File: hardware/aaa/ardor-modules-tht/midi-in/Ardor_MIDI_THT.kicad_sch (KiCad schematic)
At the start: 18 parts, among them J101 POWER INPUT + UART OUTPUT TO 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, J202 MIDI INPUT FROM DIN SOCKET, J203 METAL CASE BOND + GROUND, U201 onsemi H11L1M

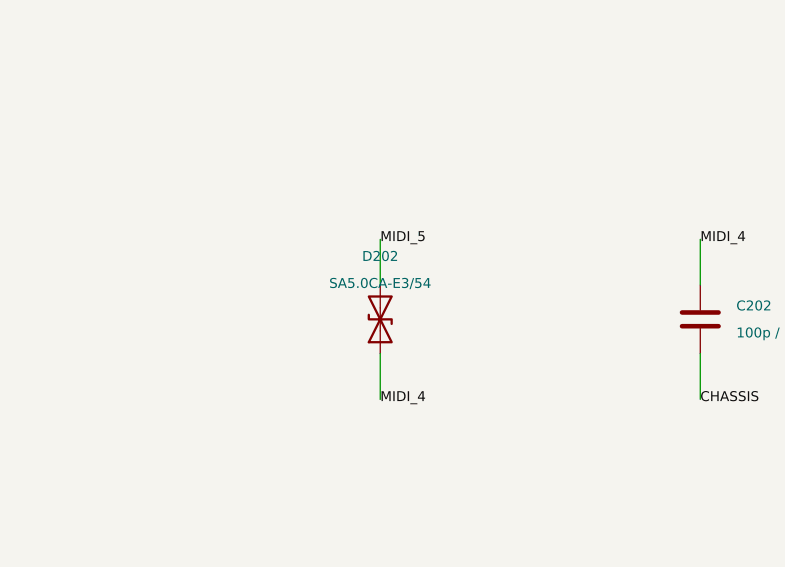
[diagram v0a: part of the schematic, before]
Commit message: fix(hardware): use Hestore TVS diodes in hand-assembly modules
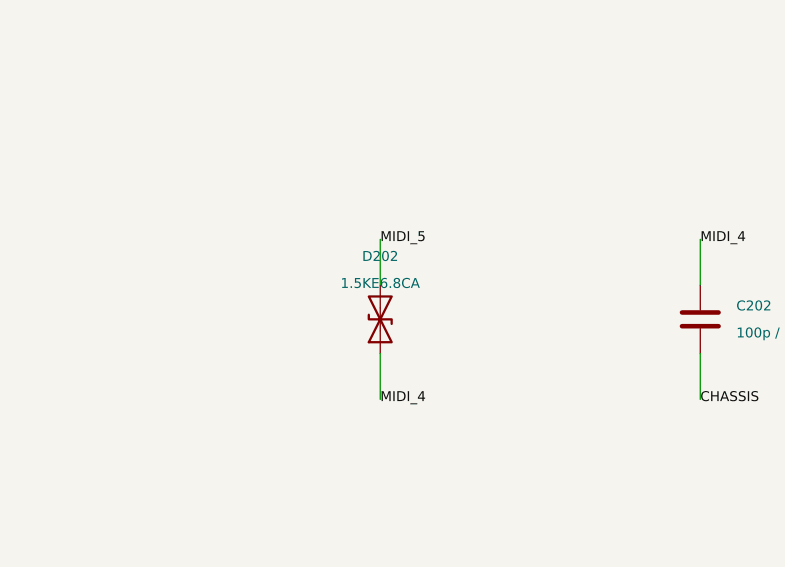
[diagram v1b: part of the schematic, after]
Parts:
- D202: value SA5.0CA-E3/54 -> 1.5KE6.8CA; footprint Diode_THT:D_DO-15_P10.16mm_Horizontal -> Ardor_THT:D_TVS_DC_1.5KE_P15.24mm; MPN Vishay SA5.0CA-E3/54 -> DC Components 1.5KE6.8CA (HESTORE 100.430.71)

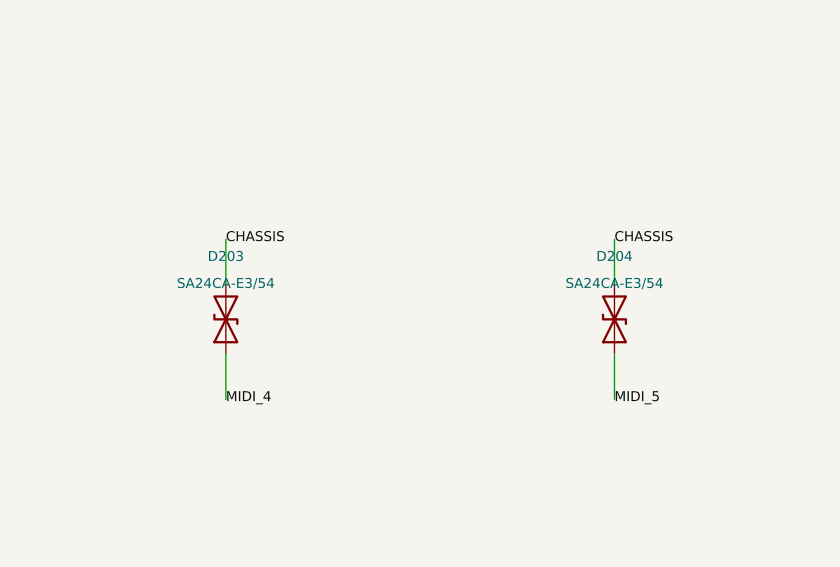
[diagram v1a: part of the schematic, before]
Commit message: feat(hardware): compact layouts and adopt Hestore module packages
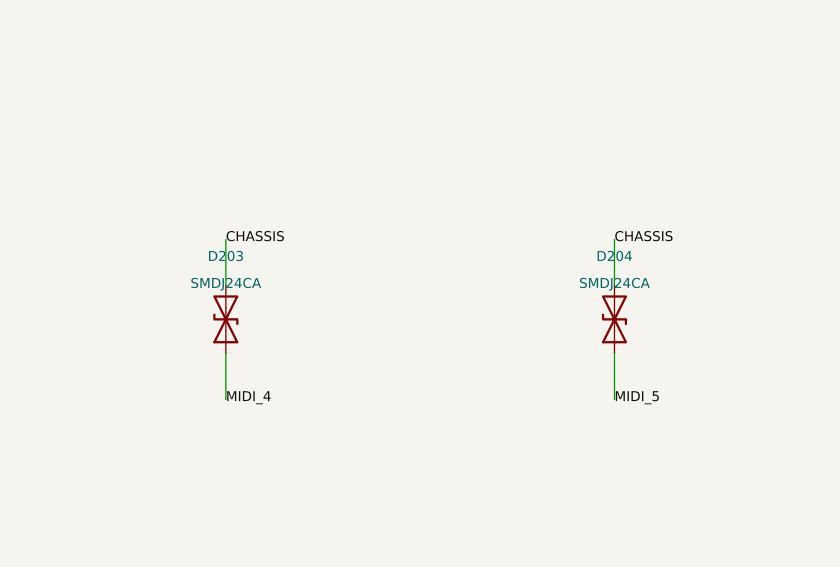
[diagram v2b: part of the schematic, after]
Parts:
- D203, D204: value SA24CA-E3/54 -> SMDJ24CA; footprint Diode_THT:D_DO-15_P10.16mm_Horizontal -> Ardor_THT:D_SMC_Bidirectional_Handsolder; MPN Vishay SA24CA-E3/54 -> Littelfuse SMDJ24CA (HESTORE 100.461.56)
